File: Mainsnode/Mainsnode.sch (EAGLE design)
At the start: 30 parts, among them IC1 LTC-1966MSOP-8, IC2 LTC-1966MSOP-8, IC3 LD117AS33TR

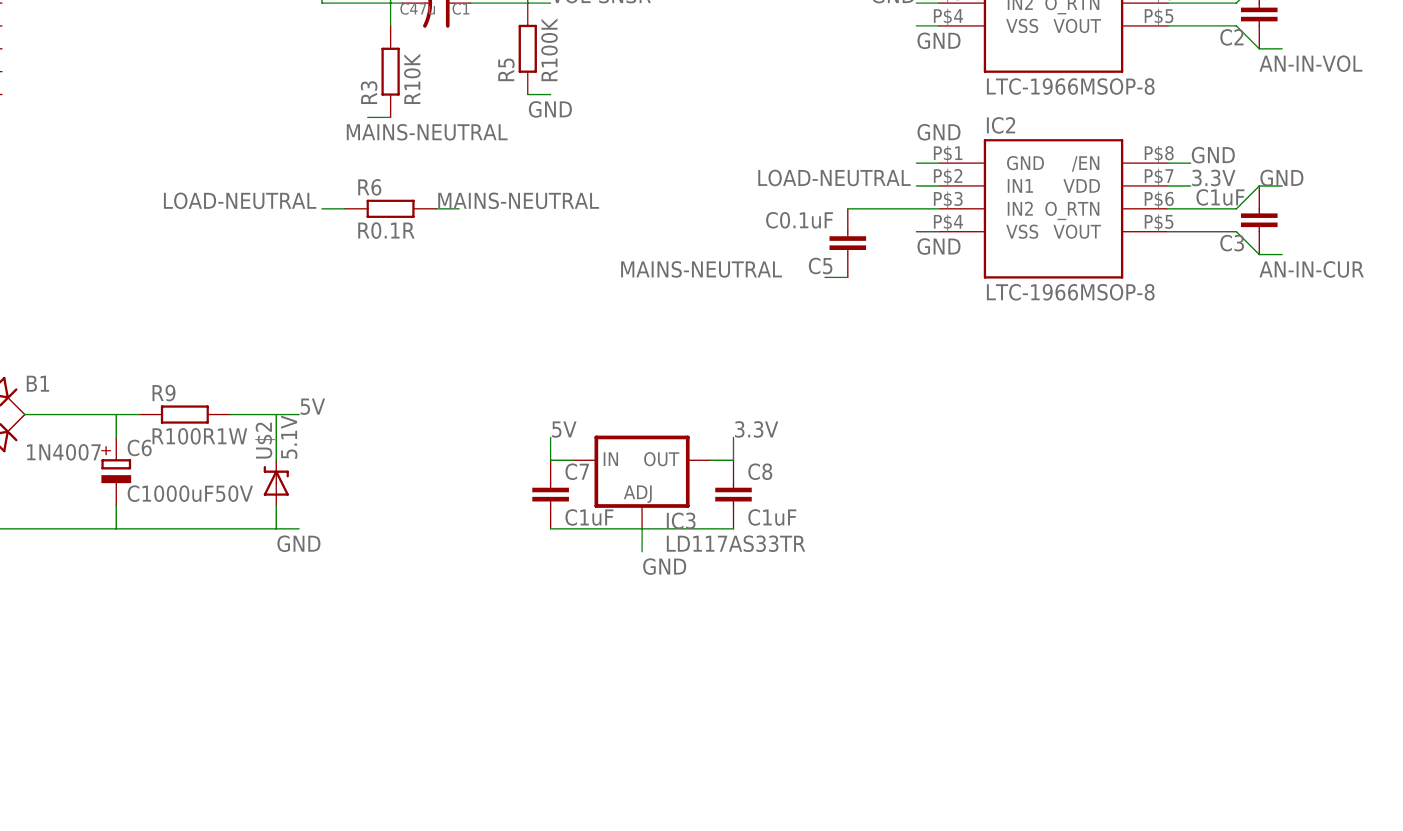
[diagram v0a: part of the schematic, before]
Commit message: Add ACS712, 5V supply, conditioner 3.3V
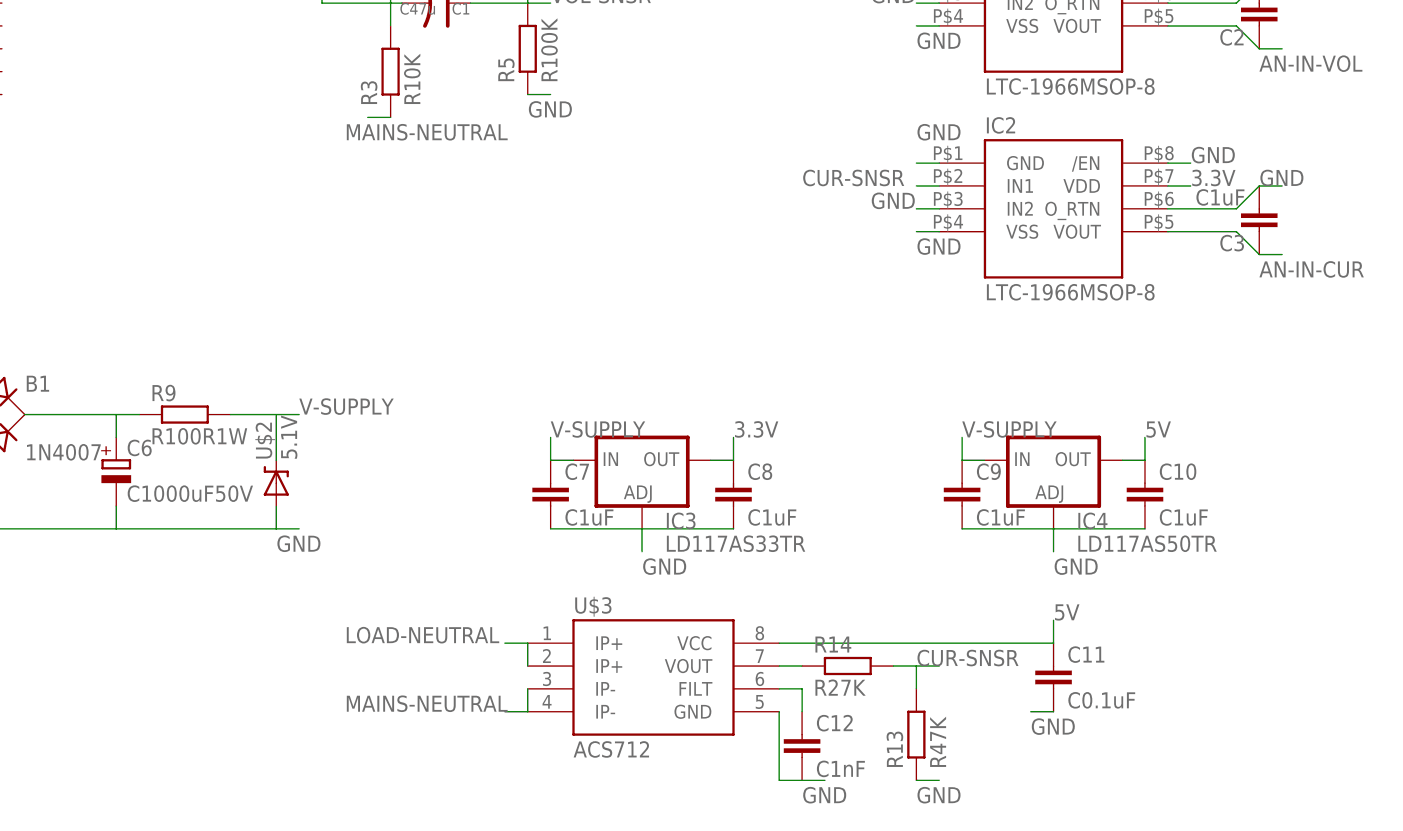
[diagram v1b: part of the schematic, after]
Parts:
- removed C5: C0.1uF, resistor:C-EUC0805
- removed R6: R0.1R, resistor:R-EU_0613/5V
- added C10, C9: C1uF, resistor:C-EUC0805
- added C11: C0.1uF, resistor:C-EUC0805
- added C12: C1nF, resistor:C-EUC0805
- added IC4: LD117AS50TR, v-reg:LD117AS50TR
- added R13: R47K, resistor:R-EU_R0603
- added R14: R27K, resistor:R-EU_R0603
- added U$3: ACS712, SparkFun-AnalogIC:ACS712
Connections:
- removed net N$2: C5.2, IC2.IN2
- new net CUR-SNSR: IC2.IN1, R13.2, R14.2
- new net N$7: C12.1, U$3.FILT
- new net N$9: R14.1, U$3.VOUT
- new net V-SUPPLY: C7.1, C9.1, IC3.IN, IC4.IN, R9.2, U$2.C
- net 5V: now also C10.1, C11.1, IC4.OUT, U$3.VCC; no longer C7.1, IC3.IN, R9.2, U$2.C
- net GND: now also C10.2, C11.2, C12.2, C9.2, IC2.IN2, IC4.ADJ, R13.1, U$3.GND
- net LOAD-NEUTRAL: now also U$3.IP+@1, U$3.IP+@2; no longer IC2.IN1, R6.1
- net MAINS-NEUTRAL: now also U$3.IP-@3, U$3.IP-@4; no longer C5.1, R6.2
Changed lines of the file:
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@@
 <part name="C1" library="OPL Eagle Library" deviceset="C-POLAR*" device="-C" value="C47u"/>
 <part name="R1" library="resistor" deviceset="R-EU_" device="0309/V" value="R10M"/>
-<part name="R6" library="resistor" deviceset="R-EU_" device="0613/5V" value="R0.1R"/>
 <part name="IC1" library="custom-tigor" deviceset="LTC-1966" device="MSOP-8"/>
 <part name="C2" library="resistor" deviceset="C-EU" device="C0805" value="C1uF"/>
 <part name="IC2" library="custom-tigor" deviceset="LTC-1966" device="MSOP-8"/>
 <part name="C3" library="resistor" deviceset="C-EU" device="C0805" value="C1uF"/>
-<part name="C5" library="resistor" deviceset="C-EU" device="C0805" value="C0.1uF"/>
 <part name="R7" library="resistor" deviceset="R-EU_" device="0309/V" value="R470K1W"/>
 <part name="R8" library="resistor" deviceset="R-EU_" device="0309/V" value="R100R1W"/>
@@
 <part name="LED-PWR" library="SparkFun-LED" deviceset="LED" device="0603"/>
 <part name="R12" library="resistor" deviceset="R-EU_" device="R0603" value="R330R"/>
+<part name="U$3" library="SparkFun-AnalogIC" deviceset="ACS712" device=""/>
+<part name="IC4" library="v-reg" deviceset="LD117A?*" device="S" technology="50TR"/>
+<part name="C9" library="resistor" deviceset="C-EU" device="C0805" value="C1uF"/>
+<part name="C10" library="resistor" deviceset="C-EU" device="C0805" value="C1uF"/>
+<part name="C11" library="resistor" deviceset="C-EU" device="C0805" value="C0.1uF"/>
+<part name="C12" library="resistor" deviceset="C-EU" device="C0805" value="C1nF"/>
+<part name="R13" library="resistor" deviceset="R-EU_" device="R0603" value="R47K"/>
+<part name="R14" library="resistor" deviceset="R-EU_" device="R0603" value="R27K"/>
 </parts>
 <sheets>
@@
 <instance part="C1" gate="C" x="215.9" y="68.58" rot="R180"/>
 <instance part="R1" gate="G$1" x="203.2" y="76.2" rot="R90"/>
-<instance part="R6" gate="G$1" x="210.82" y="45.72"/>
 <instance part="IC1" gate="G$1" x="284.48" y="68.58"/>
 <instance part="C2" gate="G$1" x="307.34" y="66.04" rot="R180"/>
 <instance part="IC2" gate="G$1" x="284.48" y="45.72"/>
 <instance part="C3" gate="G$1" x="307.34" y="43.18" rot="R180"/>
-<instance part="C5" gate="G$1" x="261.62" y="40.64" rot="R180"/>
 <instance part="R7" gate="G$1" x="147.32" y="27.94"/>
 <instance part="R8" gate="G$1" x="134.62" y="12.7"/>
@@
 <instance part="LED-PWR" gate="G$1" x="106.68" y="43.18"/>
 <instance part="R12" gate="G$1" x="106.68" y="30.48" rot="R90"/>
+<instance part="U$3" gate="G$1" x="241.3" y="-7.62"/>
+<instance part="IC4" gate="G$1" x="284.48" y="17.78"/>
+<instance part="C9" gate="G$1" x="274.32" y="15.24"/>
+<instance part="C10" gate="G$1" x="294.64" y="15.24"/>
+<instance part="C11" gate="G$1" x="284.48" y="-5.08"/>
+<instance part="C12" gate="G$1" x="256.54" y="-12.7"/>
+<instance part="R13" gate="G$1" x="269.24" y="-12.7" rot="R90"/>
+<instance part="R14" gate="G$1" x="261.62" y="-5.08"/>
 </instances>
 <busses>
@@
 <label x="104.14" y="22.86" size="1.778" layer="95"/>
 </segment>
+<segment>
+<pinref part="C9" gate="G$1" pin="2"/>
+<pinref part="IC4" gate="G$1" pin="ADJ"/>
+<wire x1="274.32" y1="10.16" x2="284.48" y2="10.16" width="0.1524" layer="91"/>
+<pinref part="C10" gate="G$1" pin="2"/>
+<wire x1="284.48" y1="10.16" x2="294.64" y2="10.16" width="0.1524" layer="91"/>
+<wire x1="284.48" y1="10.16" x2="284.48" y2="7.62" width="0.1524" layer="91"/>
+<label x="284.48" y="5.08" size="1.778" layer="95"/>
+</segment>
+<segment>
+<pinref part="C11" gate="G$1" pin="2"/>
+<wire x1="284.48" y1="-10.16" x2="281.94" y2="-10.16" width="0.1524" layer="91"/>
+<label x="281.94" y="-12.7" size="1.778" layer="95"/>
+</segment>
+<segment>
+<pinref part="U$3" gate="G$1" pin="GND"/>
+<wire x1="254" y1="-10.16" x2="254" y2="-17.78" width="0.1524" layer="91"/>
+<pinref part="C12" gate="G$1" pin="2"/>
+<wire x1="254" y1="-17.78" x2="256.54" y2="-17.78" width="0.1524" layer="91"/>
+<wire x1="256.54" y1="-17.78" x2="259.08" y2="-17.78" width="0.1524" layer="91"/>
+<label x="256.54" y="-20.32" size="1.778" layer="95"/>
+</segment>
+<segment>
+<pinref part="R13" gate="G$1" pin="1"/>
+<wire x1="269.24" y1="-17.78" x2="271.78" y2="-17.78" width="0.1524" layer="91"/>
+<label x="269.24" y="-20.32" size="1.778" layer="95"/>
+</segment>
+<segment>
+<pinref part="IC2" gate="G$1" pin="IN2"/>
+<wire x1="271.78" y1="45.72" x2="269.24" y2="45.72" width="0.1524" layer="91"/>
+<label x="264.16" y="45.72" size="1.778" layer="95"/>
+</segment>
 </net>
 <net name="RSSI" class="0">
@@
 <net name="LOAD-NEUTRAL" class="0">
 <segment>
-<pinref part="IC2" gate="G$1" pin="IN1"/>
-<wire x1="271.78" y1="48.26" x2="269.24" y2="48.26" width="0.1524" layer="91"/>
-<label x="251.46" y="48.26" size="1.778" layer="95"/>
-</segment>
-<segment>
 <pinref part="LOAD" gate="-1" pin="KL"/>
 <wire x1="231.14" y1="99.06" x2="233.68" y2="99.06" width="0.1524" layer="91"/>
@@
 </segment>
 <segment>
-<pinref part="R6" gate="G$1" pin="1"/>
-<wire x1="205.74" y1="45.72" x2="203.2" y2="45.72" width="0.1524" layer="91"/>
-<label x="185.42" y="45.72" size="1.778" layer="95"/>
+<pinref part="U$3" gate="G$1" pin="IP+@2"/>
+<pinref part="U$3" gate="G$1" pin="IP+@1"/>
+<wire x1="226.06" y1="-5.08" x2="226.06" y2="-2.54" width="0.1524" layer="91"/>
+<wire x1="226.06" y1="-2.54" x2="223.52" y2="-2.54" width="0.1524" layer="91"/>
+<label x="205.74" y="-2.54" size="1.778" layer="95"/>
 </segment>
 </net>
@@
 </segment>
 <segment>
-<pinref part="C5" gate="G$1" pin="1"/>
-<wire x1="261.62" y1="38.1" x2="259.08" y2="38.1" width="0.1524" layer="91"/>
-<label x="236.22" y="38.1" size="1.778" layer="95"/>
-</segment>
-<segment>
 <pinref part="R8" gate="G$1" pin="1"/>
 <wire x1="129.54" y1="12.7" x2="124.46" y2="12.7" width="0.1524" layer="91"/>
@@
 </segment>
 <segment>
-<pinref part="R6" gate="G$1" pin="2"/>
-<wire x1="215.9" y1="45.72" x2="218.44" y2="45.72" width="0.1524" layer="91"/>
-<label x="215.9" y="45.72" size="1.778" layer="95"/>
+<pinref part="U$3" gate="G$1" pin="IP-@3"/>
+<pinref part="U$3" gate="G$1" pin="IP-@4"/>
+<wire x1="226.06" y1="-7.62" x2="226.06" y2="-10.16" width="0.1524" layer="91"/>
+<wire x1="226.06" y1="-10.16" x2="223.52" y2="-10.16" width="0.1524" layer="91"/>
+<label x="205.74" y="-10.16" size="1.778" layer="95"/>
 </segment>
 </net>
@@
 </segment>
 </net>
-<net name="N$2" class="0">
-<segment>
-<pinref part="IC2" gate="G$1" pin="IN2"/>
-<pinref part="C5" gate="G$1" pin="2"/>
-<wire x1="271.78" y1="45.72" x2="261.62" y2="45.72" width="0.1524" layer="91"/>
-</segment>
-</net>
 <net name="N$3" class="0">
 <segment>
@@
 </segment>
 </net>
-<net name="5V" class="0">
+<net name="V-SUPPLY" class="0">
 <segment>
 <pinref part="R9" gate="G$1" pin="2"/>
@@
 <label x="228.6" y="20.32" size="1.778" layer="95"/>
 </segment>
+<segment>
+<pinref part="IC4" gate="G$1" pin="IN"/>
+<pinref part="C9" gate="G$1" pin="1"/>
+<wire x1="276.86" y1="17.78" x2="274.32" y2="17.78" width="0.1524" layer="91"/>
+<wire x1="274.32" y1="17.78" x2="274.32" y2="20.32" width="0.1524" layer="91"/>
+<label x="274.32" y="20.32" size="1.778" layer="95"/>
+</segment>
 </net>
 <net name="N$4" class="0">
@@
 </segment>
 </net>
+<net name="5V" class="0">
+<segment>
+<pinref part="IC4" gate="G$1" pin="OUT"/>
+<pinref part="C10" gate="G$1" pin="1"/>
+<wire x1="292.1" y1="17.78" x2="294.64" y2="17.78" width="0.1524" layer="91"/>
+<wire x1="294.64" y1="17.78" x2="294.64" y2="20.32" width="0.1524" layer="91"/>
+<label x="294.64" y="20.32" size="1.778" layer="95"/>
+</segment>
+<segment>
+<pinref part="U$3" gate="G$1" pin="VCC"/>
+<pinref part="C11" gate="G$1" pin="1"/>
+<wire x1="254" y1="-2.54" x2="284.48" y2="-2.54" width="0.1524" layer="91"/>
+<wire x1="284.48" y1="-2.54" x2="284.48" y2="0" width="0.1524" layer="91"/>
+<label x="284.48" y="0" size="1.778" layer="95"/>
+</segment>
+</net>
+<net name="N$7" class="0">
+<segment>
+<pinref part="U$3" gate="G$1" pin="FILT"/>
+<wire x1="254" y1="-7.62" x2="256.54" y2="-7.62" width="0.1524" layer="91"/>
+<pinref part="C12" gate="G$1" pin="1"/>
+<wire x1="256.54" y1="-7.62" x2="256.54" y2="-10.16" width="0.1524" layer="91"/>
+</segment>
+</net>
+<net name="N$9" class="0">
+<segment>
+<pinref part="U$3" gate="G$1" pin="VOUT"/>
+<pinref part="R14" gate="G$1" pin="1"/>
+<wire x1="254" y1="-5.08" x2="256.54" y2="-5.08" width="0.1524" layer="91"/>
+</segment>
+</net>
+<net name="CUR-SNSR" class="0">
+<segment>
+<pinref part="R14" gate="G$1" pin="2"/>
+<pinref part="R13" gate="G$1" pin="2"/>
+<wire x1="266.7" y1="-5.08" x2="269.24" y2="-5.08" width="0.1524" layer="91"/>
+<wire x1="269.24" y1="-5.08" x2="269.24" y2="-7.62" width="0.1524" layer="91"/>
+<wire x1="269.24" y1="-5.08" x2="271.78" y2="-5.08" width="0.1524" layer="91"/>
+<label x="269.24" y="-5.08" size="1.778" layer="95"/>
+</segment>
+<segment>
+<pinref part="IC2" gate="G$1" pin="IN1"/>
+<wire x1="271.78" y1="48.26" x2="269.24" y2="48.26" width="0.1524" layer="91"/>
+<label x="256.54" y="48.26" size="1.778" layer="95"/>
+</segment>
+</net>
